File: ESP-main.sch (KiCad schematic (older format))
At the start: 14 parts, among them Q201 BSS138, Q202 BSS138, SW201 EN, SW203 FLASH, U201 ESP32-WROVER

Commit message: current
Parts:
- added U202: MIC803, Package_TO_SOT_SMD:SOT-23, symbol special-ics:MIC803
- C202: value 3.3u -> 1u
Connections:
- net +3V3: now also U202.3 (VCC)
- net EN: now also U202.2 (RST)
- net GND: now also U202.1 (GND)
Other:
- moved on the sheet: C201
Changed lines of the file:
@@
 Title "ESP32 Eurorack Audio Module"
 Date "2019-03-27"
-Rev "B2-public"
+Rev "C"
 Comp "(c) Robert Manzke 2019"
 Comment1 "https://creativecommons.org/licenses/by-nc-sa/4.0/"
@@
 P 3750 2400
 F 0 "C202" H 3865 2446 50  0000 L CNN
-F 1 "3.3u" H 3865 2355 50  0000 L CNN
+F 1 "1u" H 3865 2355 50  0000 L CNN
 F 2 "Capacitor_SMD:C_0603_1608Metric" H 3788 2250 50  0001 C CNN
 F 3 "~" H 3750 2400 50  0001 C CNN
@@
 L power:+3.3V #PWR0205
 U 1 1 5B66F875
-P 3300 2100
-F 0 "#PWR0205" H 3300 1950 50  0001 C CNN
-F 1 "+3.3V" H 3315 2273 50  0000 C CNN
-F 2 "" H 3300 2100 50  0001 C CNN
-F 3 "" H 3300 2100 50  0001 C CNN
-	1    3300 2100
+P 2000 2100
+F 0 "#PWR0205" H 2000 1950 50  0001 C CNN
+F 1 "+3.3V" H 2015 2273 50  0000 C CNN
+F 2 "" H 2000 2100 50  0001 C CNN
+F 3 "" H 2000 2100 50  0001 C CNN
+	1    2000 2100
 	1    0    0    -1
 $EndComp
@@
 L power:GND #PWR0207
 U 1 1 5B66F9C7
-P 3300 2700
-F 0 "#PWR0207" H 3300 2450 50  0001 C CNN
-F 1 "GND" H 3305 2527 50  0000 C CNN
-F 2 "" H 3300 2700 50  0001 C CNN
-F 3 "" H 3300 2700 50  0001 C CNN
-	1    3300 2700
+P 2000 2700
+F 0 "#PWR0207" H 2000 2450 50  0001 C CNN
+F 1 "GND" H 2005 2527 50  0000 C CNN
+F 2 "" H 2000 2700 50  0001 C CNN
+F 3 "" H 2000 2700 50  0001 C CNN
+	1    2000 2700
 	1    0    0    -1
 $EndComp
@@
 L Device:C C201
 U 1 1 5B66FF56
-P 3300 2400
-F 0 "C201" H 3415 2446 50  0000 L CNN
-F 1 "10u" H 3415 2355 50  0000 L CNN
-F 2 "Capacitor_SMD:C_0805_2012Metric" H 3338 2250 50  0001 C CNN
-F 3 "~" H 3300 2400 50  0001 C CNN
-	1    3300 2400
+P 2000 2400
+F 0 "C201" H 2115 2446 50  0000 L CNN
+F 1 "10u" H 2115 2355 50  0000 L CNN
+F 2 "Capacitor_SMD:C_0805_2012Metric" H 2038 2250 50  0001 C CNN
+F 3 "~" H 2000 2400 50  0001 C CNN
+	1    2000 2400
 	1    0    0    -1
 $EndComp
@@
 $EndComp
 Wire Wire Line
-	3300 2550 3300 2700
-Wire Wire Line
-	3300 2100 3300 2250
+	2000 2550 2000 2700
+Wire Wire Line
+	2000 2100 2000 2250
 Text HLabel 7300 3150 2    50   BiDi ~ 0
 IO4
@@
 Wire Notes Line
 	8050 4100 2600 4100
+$Comp
+L special-ics:MIC803 U202
+U 1 1 5CA3F4DA
+P 2950 2350
+F 0 "U202" H 2672 2596 50  0000 R CNN
+F 1 "MIC803" H 2672 2505 50  0000 R CNN
+F 2 "Package_TO_SOT_SMD:SOT-23" H 2950 2350 50  0001 C CNN
+F 3 "" H 2950 2350 50  0001 C CNN
+	1    2950 2350
+	1    0    0    -1
+$EndComp
+$Comp
+L power:+3.3V #PWR0109
+U 1 1 5CA450EC
+P 2950 1650
+F 0 "#PWR0109" H 2950 1500 50  0001 C CNN
+F 1 "+3.3V" H 2965 1823 50  0000 C CNN
+F 2 "" H 2950 1650 50  0001 C CNN
+F 3 "" H 2950 1650 50  0001 C CNN
+	1    2950 1650
+	1    0    0    -1
+$EndComp
+Wire Wire Line
+	2950 1650 2950 1750
+$Comp
+L power:GND #PWR0110
+U 1 1 5CA47446
+P 2950 2700
+F 0 "#PWR0110" H 2950 2450 50  0001 C CNN
+F 1 "GND" H 2955 2527 50  0000 C CNN
+F 2 "" H 2950 2700 50  0001 C CNN
+F 3 "" H 2950 2700 50  0001 C CNN
+	1    2950 2700
+	1    0    0    -1
+$EndComp
+Wire Wire Line
+	2950 2550 2950 2700
+Wire Wire Line
+	3750 2150 3400 2150
 $EndSCHEMATC

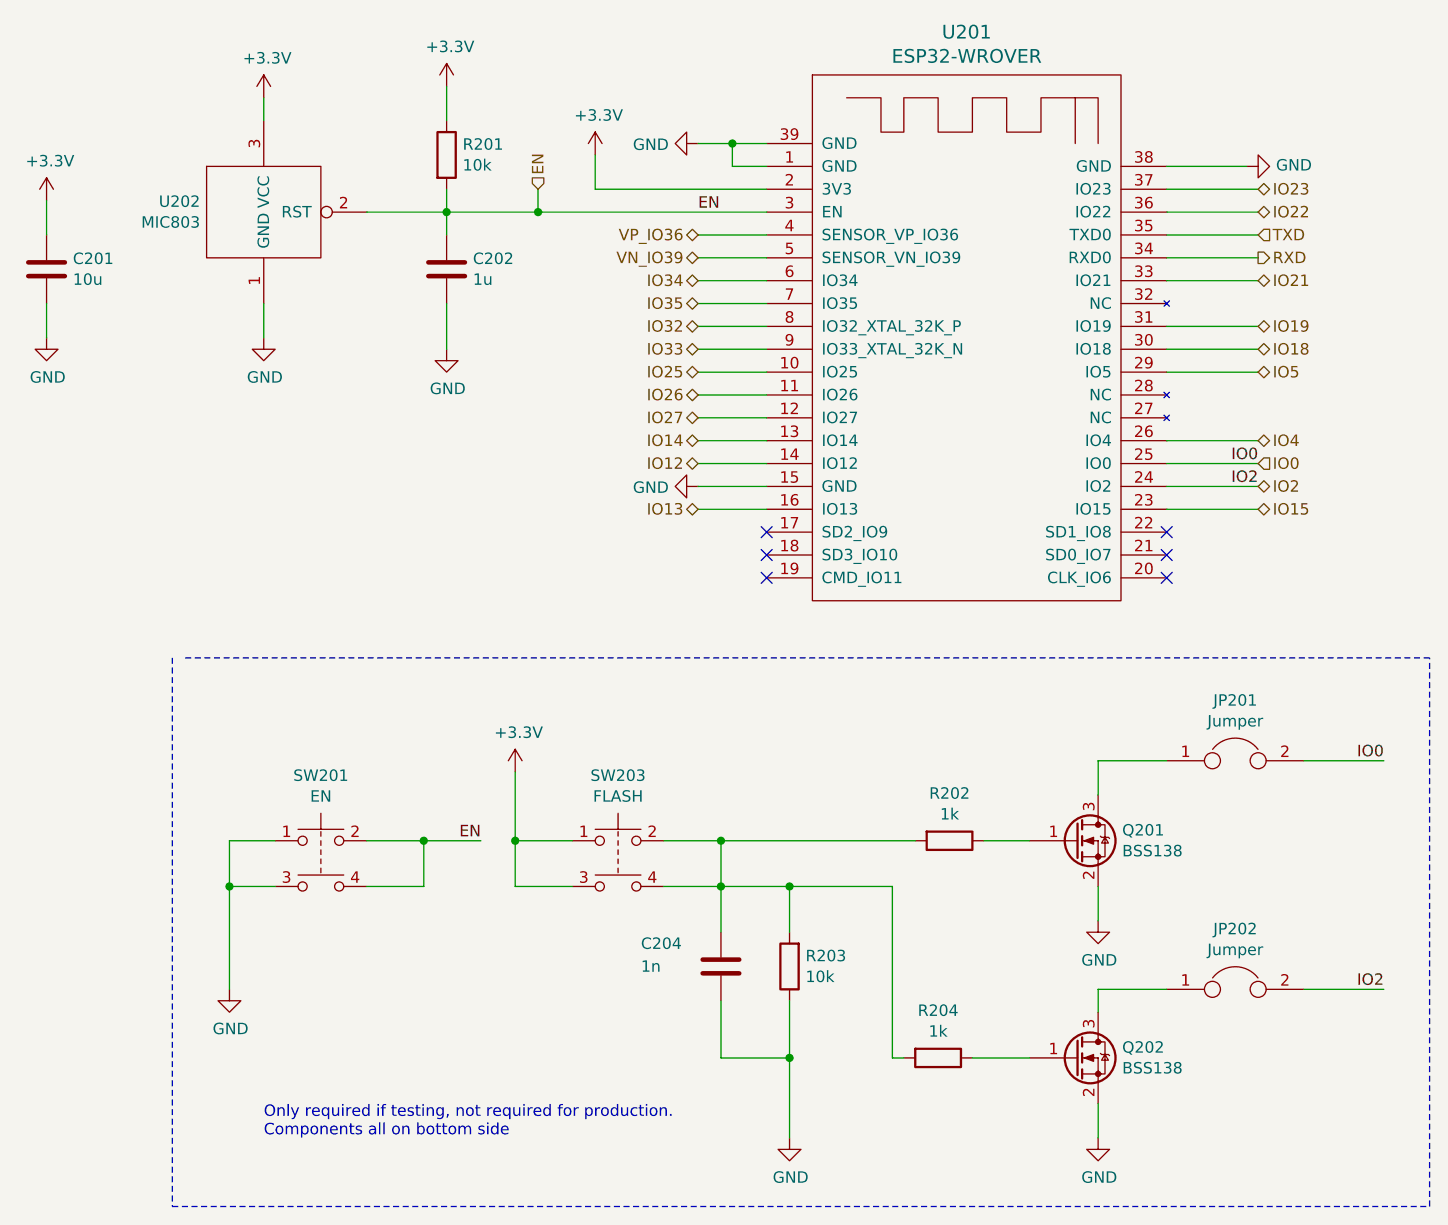
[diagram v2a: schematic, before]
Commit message: cleaned up schematic
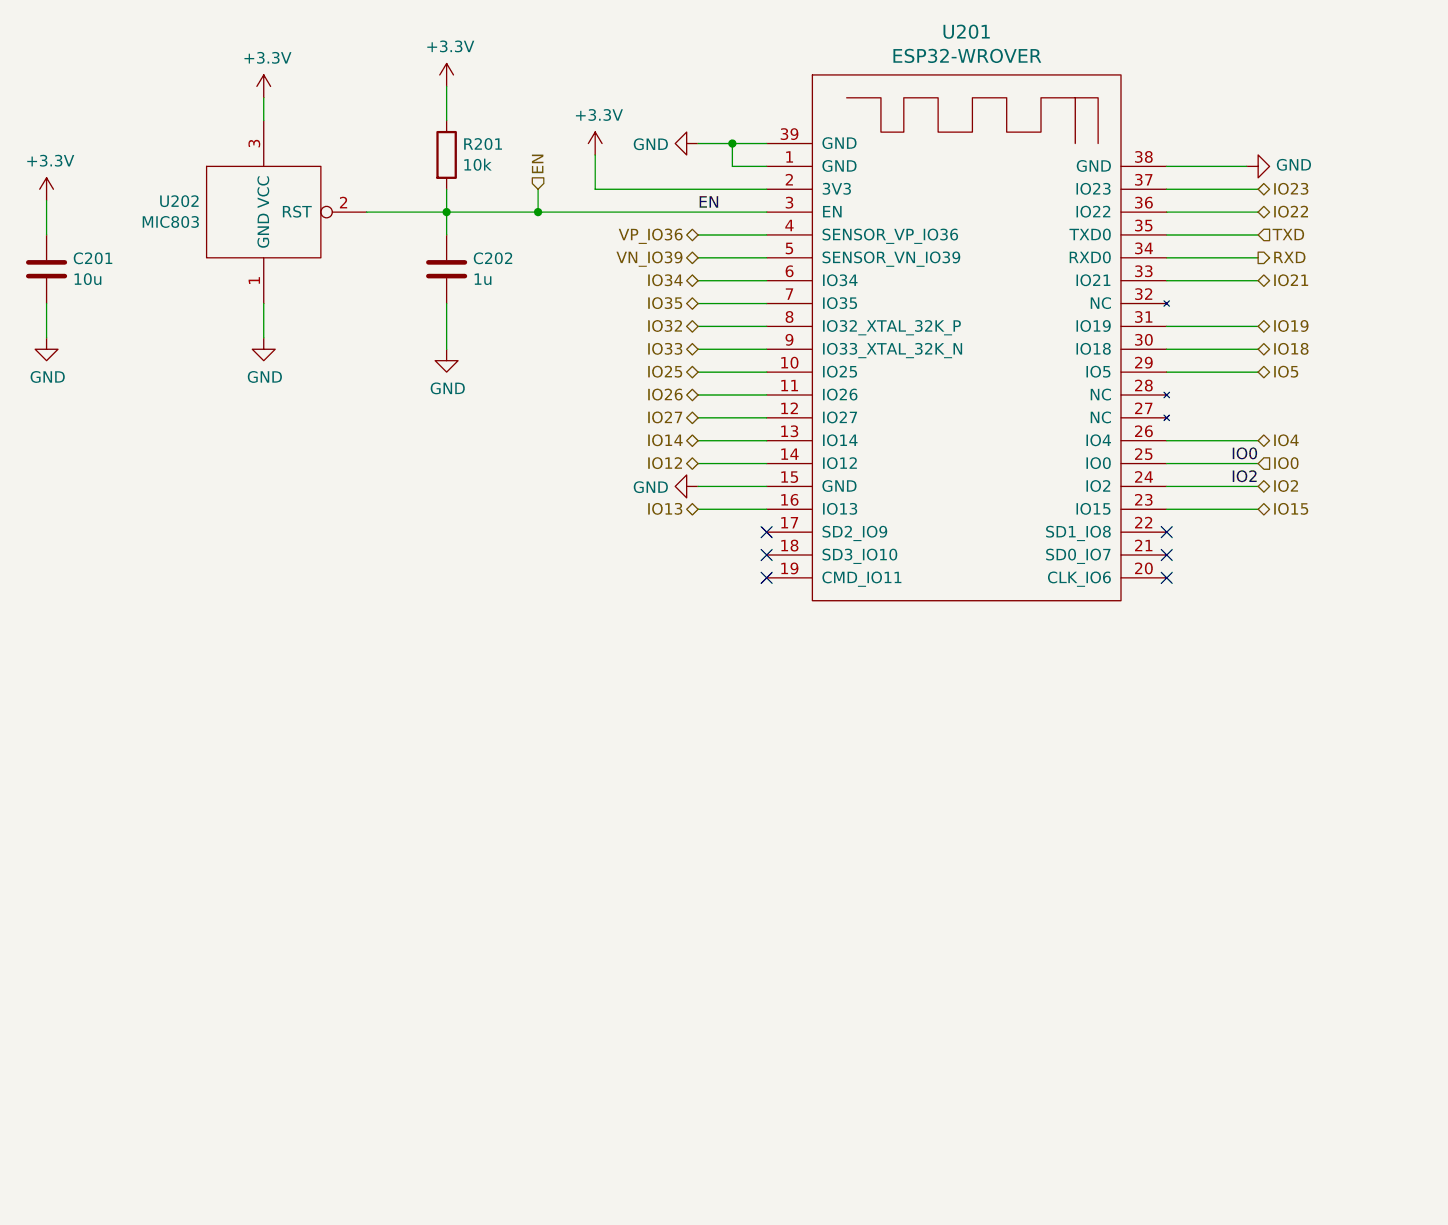
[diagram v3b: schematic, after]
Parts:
- removed C204: 1n, Capacitor_SMD:C_0603_1608Metric, symbol Device:C
- removed JP201, JP202: Jumper, Jumper:SolderJumper-2_P1.3mm_Open_TrianglePad1.0x1.5mm, symbol Device:Jumper
- removed Q201, Q202: BSS138, Package_TO_SOT_SMD:SOT-23, symbol Transistor_FET:BSS138
- removed R202, R204: 1k, Resistor_SMD:R_0603_1608Metric, symbol Device:R
- removed R203: 10k, Resistor_SMD:R_0603_1608Metric, symbol Device:R
- removed SW201: EN, Button_Switch_SMD:SW_SPST_PTS810, symbol Switch:SW_Push_Dual
- removed SW203: FLASH, Button_Switch_SMD:SW_SPST_PTS810, symbol Switch:SW_Push_Dual
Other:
- note removed: "Only required if testing, not required for production.\nComponents all on bottom side"
